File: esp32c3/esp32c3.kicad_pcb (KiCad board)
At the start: 2 copper layers, 38.4 x 27.2 mm, 29 parts, among them J1 A1501WR-S-2P, J2 Conn_01x06, J3 Conn_01x05, SW1 wake up, U1 ESP32-C3-WROOM-02, U2 AHT10, U3 LIS2DH, U4 HX6306

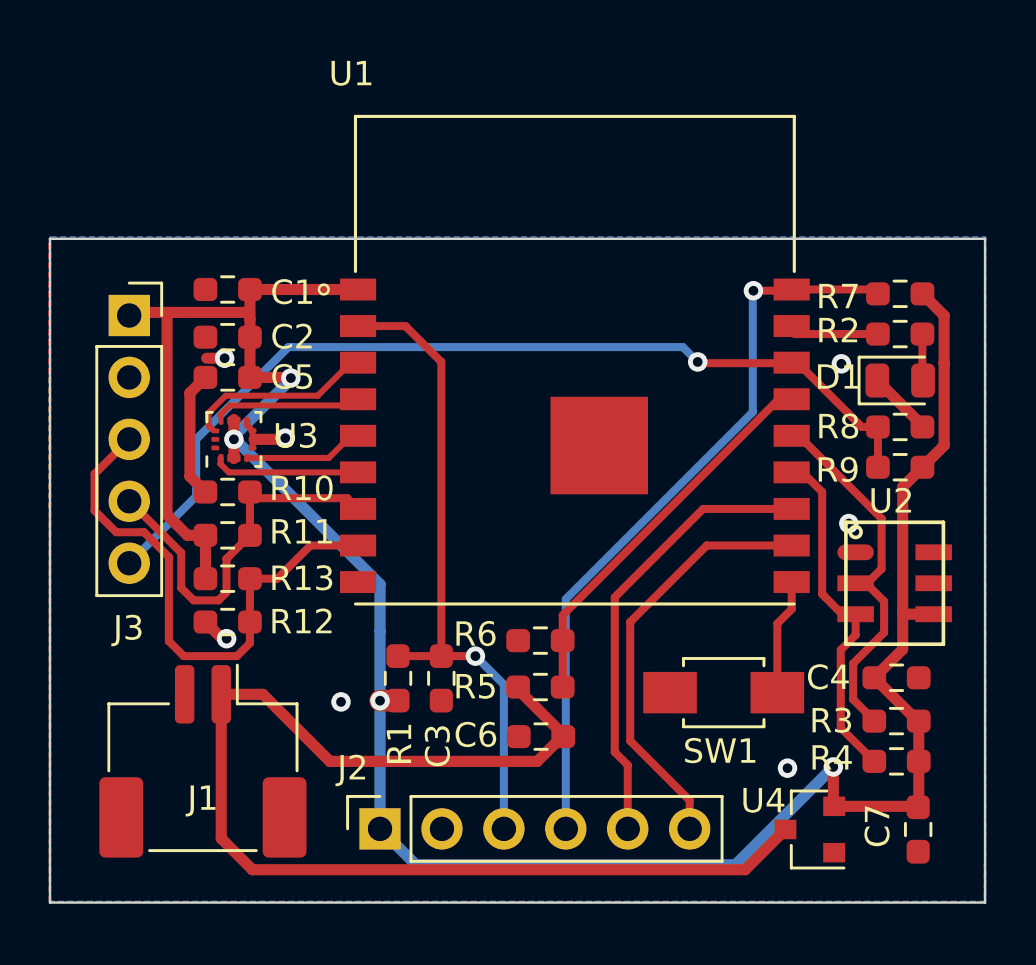
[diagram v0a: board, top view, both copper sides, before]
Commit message: Complete LIS2DH12 modification
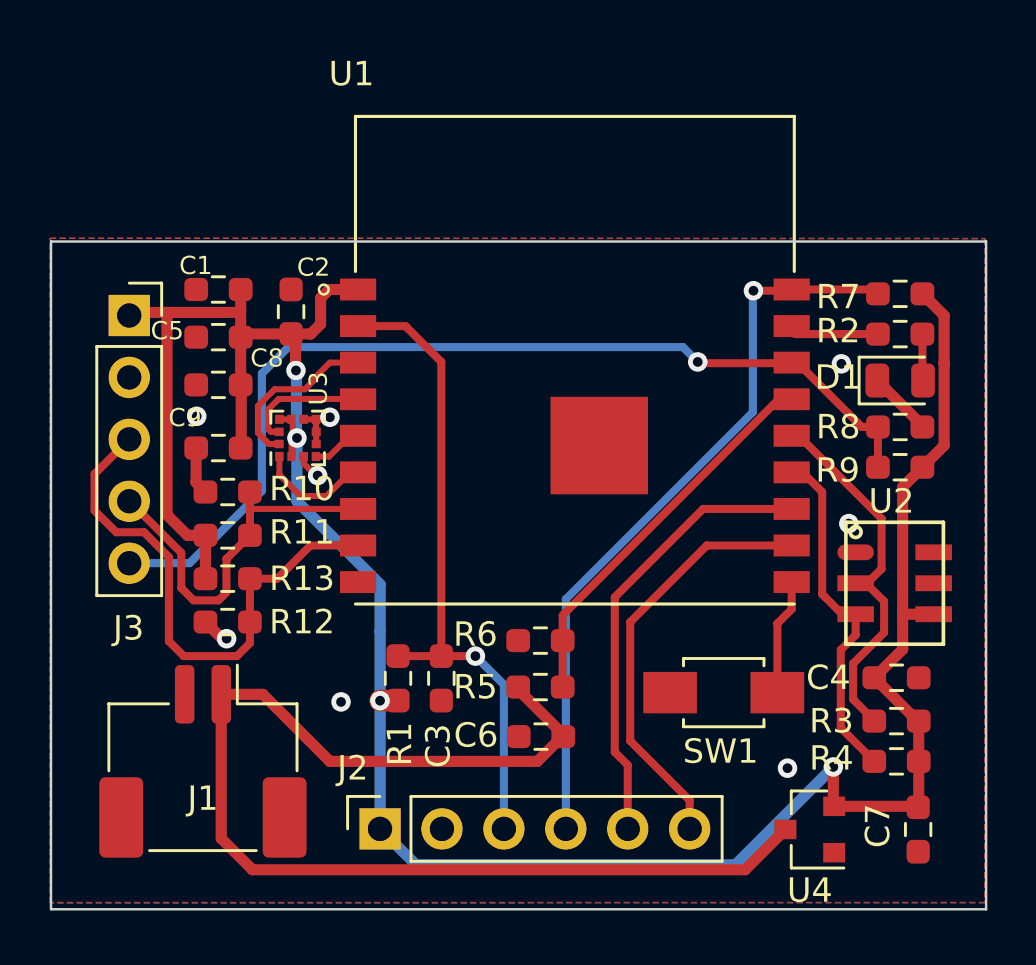
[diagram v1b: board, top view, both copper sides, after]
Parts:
- added C8: 0.1uF, Resistor_SMD:R_0603_1608Metric_Pad0.98x0.95mm_HandSolder, F.Cu at (47.9, 75.0)
- added C9: 0.1uF, Resistor_SMD:R_0603_1608Metric_Pad0.98x0.95mm_HandSolder, F.Cu at (47.9, 77.6)
- C5: value 100nF -> 10uF
- U3: footprint Package_LGA:LGA-14_2x2mm_P0.35mm_LayoutBorder3x4y -> Package_LGA:LGA-12_2x2mm_P0.5mm
- moved C2 2.80 mm to (50.9, 72.0), turned to 90 degrees
- moved U3 2.62 mm to (51.1, 77.2)
- moved C5 1.69 mm to (47.9, 73.0)
- moved C1 0.38 mm to (47.9, 71.1)
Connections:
- U3 pad 3: 3.3V -> GND
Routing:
- net GND: track 12.3 -> 8.98 mm, vias 7 -> 8
- net SDA: track 4.92 -> 2.55 mm
- net 3.3V: track 102.8 -> 105.1 mm
- net IO2: track 38.8 -> 40.2 mm
- net SCL: track 6.03 -> 5.19 mm
- net INT2: track 5.98 -> 5.17 mm
- net INT1: track 7.74 -> 7.05 mm
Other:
- board size 38.4 x 27.2 mm -> 38.4 x 27.4 mm
